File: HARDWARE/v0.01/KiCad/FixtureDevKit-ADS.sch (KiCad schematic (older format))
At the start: 54 parts, among them J16 ADS_48, J17 ADS_48, J18 ADS_4A, J19 ADS_4A, J20 ADS_48, J21 ADS_4A, J22 ADS, J23 ADS, J24 ADS_49, J25 ADS_49, J26 ADS_49, J27 ADS_4B, J28 ADS_4B, J29 ADS_4B, U1 ADS1015IDGST, U2 ADS1015IDGST, U3 ADS1015IDGST, U4 ADS1015IDGST

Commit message: more PCB layout
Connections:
- net C4-VCC-3V3: now also J16.1 (Pin_1), J17.1 (Pin_1); no longer J16.4 (Pin_4), J17.4 (Pin_4)
- net GND: now also J16.2 (Pin_2), J17.2 (Pin_2); no longer J16.3 (Pin_3), J17.3 (Pin_3)
- net I2C-SCK: now also J16.4 (Pin_4), J17.4 (Pin_4); no longer J16.1 (Pin_1), J17.1 (Pin_1)
- net I2C-SDA: now also J16.3 (Pin_3), J17.3 (Pin_3); no longer J16.2 (Pin_2), J17.2 (Pin_2)
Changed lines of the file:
@@
 L Conn_01x04 J16
 U 1 1 59F16A10
-P 1350 2800
-F 0 "J16" H 1350 3000 50  0000 C CNN
-F 1 "ADS_48" H 1350 2500 50  0000 C CNN
-F 2 "Pin_Headers:Pin_Header_Straight_1x04_Pitch2.54mm" H 1350 2800 50  0001 C CNN
-F 3 "" H 1350 2800 50  0001 C CNN
-	1    1350 2800
-	0    1    -1   0
+P 1250 2800
+F 0 "J16" H 1250 3000 50  0000 C CNN
+F 1 "ADS_48" H 1250 2500 50  0000 C CNN
+F 2 "Pin_Headers:Pin_Header_Straight_1x04_Pitch2.54mm" H 1250 2800 50  0001 C CNN
+F 3 "" H 1250 2800 50  0001 C CNN
+	1    1250 2800
+	0    -1   -1   0
 $EndComp
 Text Label 1150 3050 3    60   ~ 0
@@
 L Conn_01x04 J17
 U 1 1 59F183CB
-P 1350 4850
-F 0 "J17" H 1350 5050 50  0000 C CNN
-F 1 "ADS_48" H 1350 4550 50  0000 C CNN
-F 2 "Pin_Headers:Pin_Header_Straight_1x04_Pitch2.54mm" H 1350 4850 50  0001 C CNN
-F 3 "" H 1350 4850 50  0001 C CNN
-	1    1350 4850
-	0    1    1    0
+P 1250 4850
+F 0 "J17" H 1250 5050 50  0000 C CNN
+F 1 "ADS_48" H 1250 4550 50  0000 C CNN
+F 2 "Pin_Headers:Pin_Header_Straight_1x04_Pitch2.54mm" H 1250 4850 50  0001 C CNN
+F 3 "" H 1250 4850 50  0001 C CNN
+	1    1250 4850
+	0    -1   1    0
 $EndComp
 Text Label 1150 4600 1    60   ~ 0

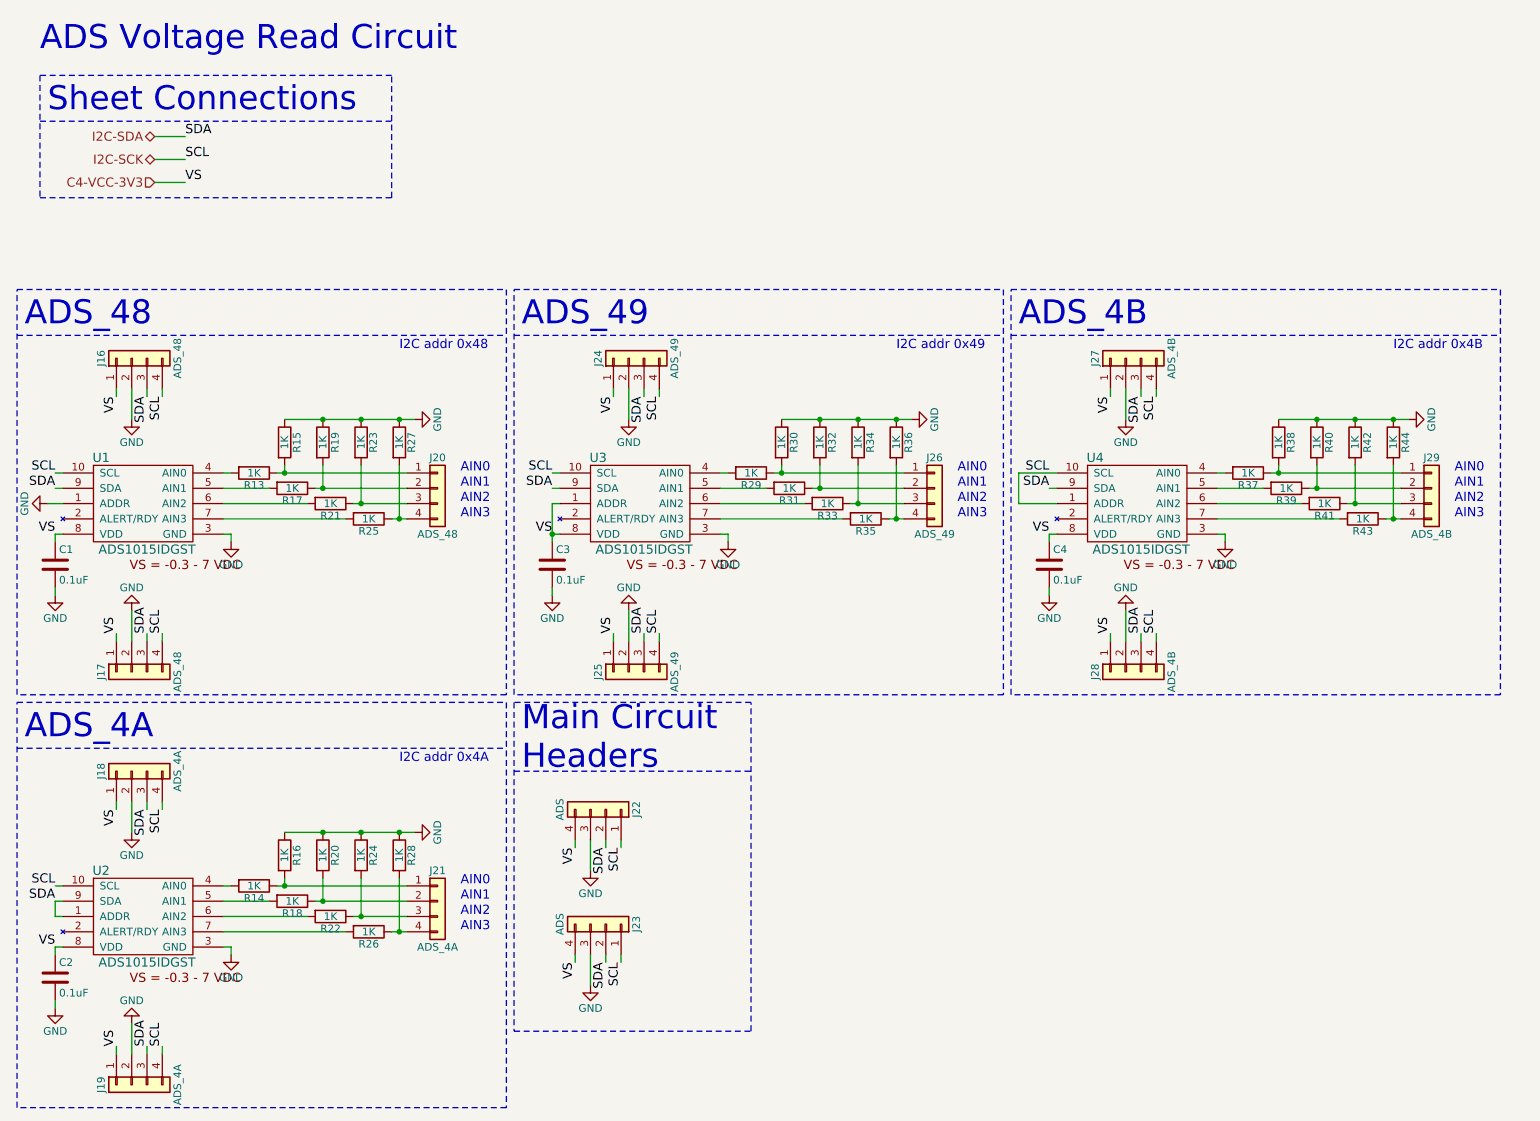
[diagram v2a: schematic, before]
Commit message: quasi-redoing entire schematic and layout
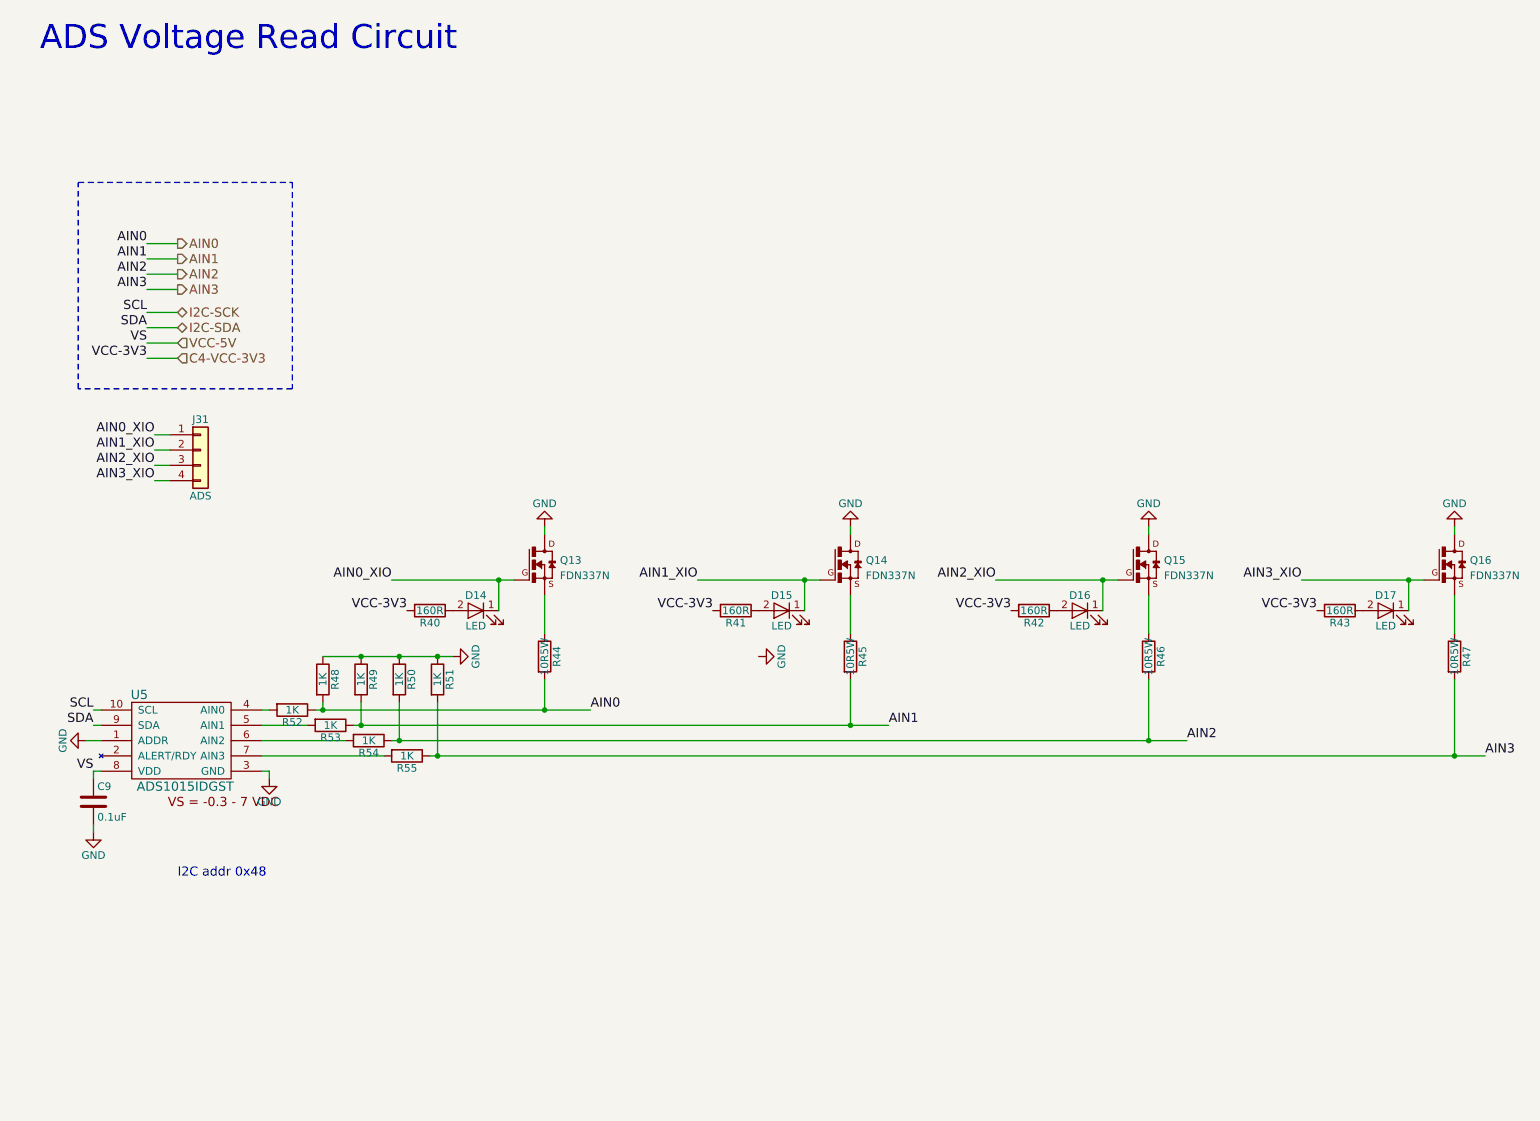
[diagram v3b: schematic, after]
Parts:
- removed C2, C3, C4: 0.1uF, Capacitors_SMD:C_0805_HandSoldering, symbol C
- removed J16, J17, J20: ADS_48, Pin_Headers:Pin_Header_Straight_1x04_Pitch2.54mm, symbol Conn_01x04
- removed J18, J19, J21: ADS_4A, Pin_Headers:Pin_Header_Straight_1x04_Pitch2.54mm, symbol Conn_01x04
- removed J22, J23: ADS, Pin_Headers:Pin_Header_Straight_1x04_Pitch2.54mm, symbol Conn_01x04
- removed J24, J25, J26: ADS_49, Pin_Headers:Pin_Header_Straight_1x04_Pitch2.54mm, symbol Conn_01x04
- removed J27, J28, J29: ADS_4B, Pin_Headers:Pin_Header_Straight_1x04_Pitch2.54mm, symbol Conn_01x04
- removed R14, R16, R18, R20, R22, R24, R26, R28, R29, R30, R31, R32, R33, R34, R35, R36, R37, R38, R39: 1K, Resistors_SMD:R_0805_HandSoldering, symbol R
- removed U2, U3, U4: ADS1015IDGST, ADS1015IDGST:SOP50P490X110-10N, symbol ADS1015IDGST
- added D14, D15, D16, D17: LED, 1206:1206, symbol LED
- added J31: ADS, Pin_Headers:Pin_Header_Straight_1x04_Pitch2.54mm, symbol Conn_01x04
- added Q13, Q14, Q15, Q16: FDN337N, FDN337N:SSOT-3, symbol FDN337N
- added R45, R46, R47: 10R5W, RES_TWM3J560E:RES_TWM3J560E, symbol R
- R40, R41, R42, R43: value 1K -> 160R
- R44: value 1K -> 10R5W; footprint Resistors_SMD:R_0805_HandSoldering -> RES_TWM3J560E:RES_TWM3J560E
- renumbered C1 to C9, R15 to R48, R19 to R49, R23 to R50, R27 to R51, R13 to R52, R17 to R53, R21 to R54, R25 to R55, U1 to U5
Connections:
- net C4-VCC-3V3: now also R40.2, R41.2, R42.2, R43.2; no longer C9.1, U5.8 (VDD)
- net GND: now also Q13.3 (D), Q14.3 (D), Q15.3 (D), Q16.3 (D); no longer R40.1, R42.1, R44.1
- net AIN0: now reaches R48.2, R52.1
- net AIN0: now also R44.2
- net AIN1: now reaches R49.2, R53.1
- net AIN1: now also R45.2
- net AIN2: now reaches R50.2, R54.1
- net AIN2: now also R46.2
- net AIN3: now reaches R51.2, R55.1
- net AIN3: now also R47.2
- net at R41.1: now also D15.2 (A); no longer R42.2
- net at R43.1: now also D17.2 (A); no longer R44.2
- new net: Q13.2 (S), R44.1
- new net: D14.2 (A), R40.1
- new net: Q14.2 (S), R45.1
- new net: Q15.2 (S), R46.1
- new net: D16.2 (A), R42.1
- new net: Q16.2 (S), R47.1
- new net AIN0_XIO: D14.1 (K), J31.1 (Pin_1), Q13.1 (G)
- new net AIN1_XIO: D15.1 (K), J31.2 (Pin_2), Q14.1 (G)
- new net AIN2_XIO: D16.1 (K), J31.3 (Pin_3), Q15.1 (G)
- new net AIN3_XIO: D17.1 (K), J31.4 (Pin_4), Q16.1 (G)
- new net VCC-5V: C9.1, U5.8 (VDD)
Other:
- note removed: "ADS_48"
- note removed: "ADS_49\n"
- note removed: "ADS_4A"
- note removed: "ADS_4B\n"
- note removed: "AIN0"
- note removed: "AIN1"
- note removed: "AIN2"
- note removed: "AIN3"
- note removed: "I2C addr 0x49"
- note removed: "I2C addr 0x4A"
- note removed: "I2C addr 0x4B"
- note removed: "Main Circuit\nHeaders"
- note removed: "Sheet Connections"
- moved on the sheet: C9, R48, R49, R50, R51, R52, R53, R54, R55, U5

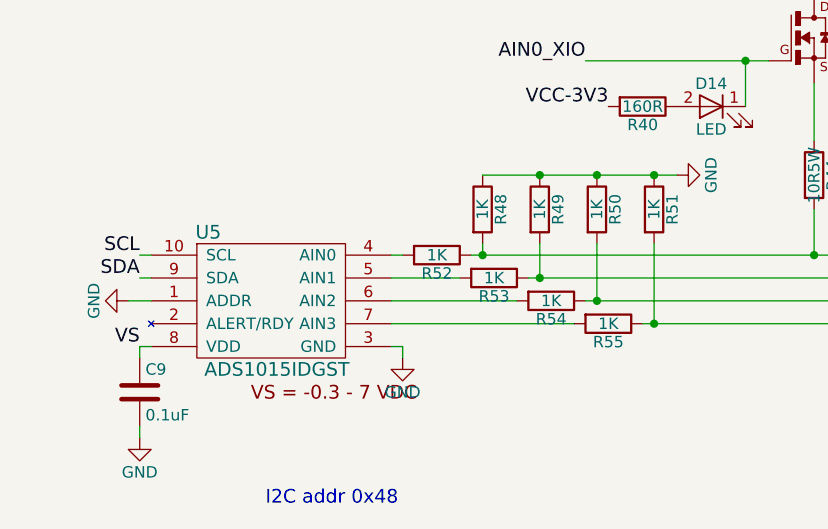
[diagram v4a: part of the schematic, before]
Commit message: updating layout footprints and board outline
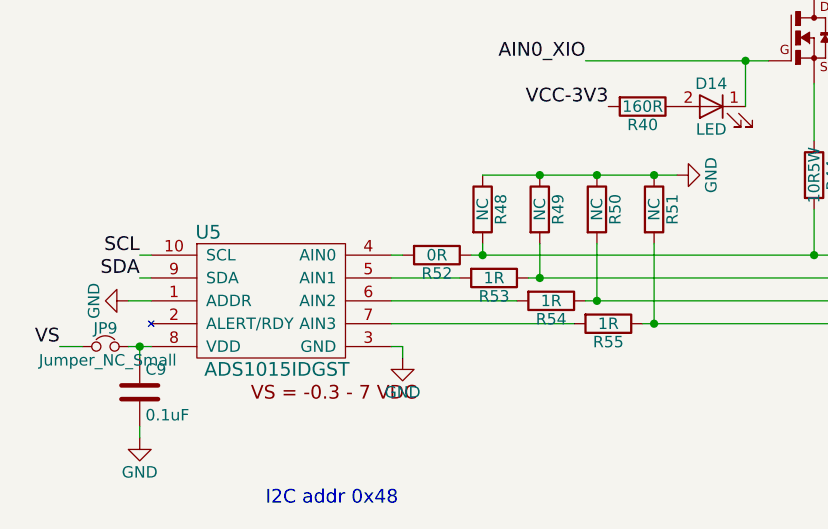
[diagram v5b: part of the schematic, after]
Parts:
- added JP9: Jumper_NC_Small, ConnectedCutJumper:connectedCutJumper, symbol Jumper_NC_Small
- R48, R49, R50, R51: value 1K -> NC
- R52: value 1K -> 0R
- R53, R54, R55: value 1K -> 1R
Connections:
- net VCC-5V: now also JP9.1; no longer C9.1, U5.8 (VDD)
- new net: C9.1, JP9.2, U5.8 (VDD)
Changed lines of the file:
@@
 Text Label 1000 5200 2    60   ~ 0
 SDA
-Text Label 1000 5500 2    60   ~ 0
+Text Label 650  5500 2    60   ~ 0
 VS
 Wire Wire Line
-	1000 5500 1050 5500
+	950  5500 1050 5500
 Wire Wire Line
 	1000 5200 1050 5200
@@
 P 2300 5100
 F 0 "R52" V 2380 5100 50  0000 C CNN
-F 1 "1K" V 2300 5100 50  0000 C CNN
+F 1 "0R" V 2300 5100 50  0000 C CNN
 F 2 "Resistors_SMD:R_0805_HandSoldering" V 2230 5100 50  0001 C CNN
 F 3 "" H 2300 5100 50  0001 C CNN
@@
 P 2500 4900
 F 0 "R48" V 2580 4900 50  0000 C CNN
-F 1 "1K" V 2500 4900 50  0000 C CNN
+F 1 "NC" V 2500 4900 50  0000 C CNN
 F 2 "Resistors_SMD:R_0805_HandSoldering" V 2430 4900 50  0001 C CNN
 F 3 "" H 2500 4900 50  0001 C CNN
@@
 P 3050 5400
 F 0 "R55" V 3130 5400 50  0000 C CNN
-F 1 "1K" V 3050 5400 50  0000 C CNN
+F 1 "1R" V 3050 5400 50  0000 C CNN
 F 2 "Resistors_SMD:R_0805_HandSoldering" V 2980 5400 50  0001 C CNN
 F 3 "" H 3050 5400 50  0001 C CNN
@@
 P 2800 5300
 F 0 "R54" V 2880 5300 50  0000 C CNN
-F 1 "1K" V 2800 5300 50  0000 C CNN
+F 1 "1R" V 2800 5300 50  0000 C CNN
 F 2 "Resistors_SMD:R_0805_HandSoldering" V 2730 5300 50  0001 C CNN
 F 3 "" H 2800 5300 50  0001 C CNN
@@
 P 2550 5200
 F 0 "R53" V 2630 5200 50  0000 C CNN
-F 1 "1K" V 2550 5200 50  0000 C CNN
+F 1 "1R" V 2550 5200 50  0000 C CNN
 F 2 "Resistors_SMD:R_0805_HandSoldering" V 2480 5200 50  0001 C CNN
 F 3 "" H 2550 5200 50  0001 C CNN
@@
 P 3250 4900
 F 0 "R51" V 3330 4900 50  0000 C CNN
-F 1 "1K" V 3250 4900 50  0000 C CNN
+F 1 "NC" V 3250 4900 50  0000 C CNN
 F 2 "Resistors_SMD:R_0805_HandSoldering" V 3180 4900 50  0001 C CNN
 F 3 "" H 3250 4900 50  0001 C CNN
@@
 P 3000 4900
 F 0 "R50" V 3080 4900 50  0000 C CNN
-F 1 "1K" V 3000 4900 50  0000 C CNN
+F 1 "NC" V 3000 4900 50  0000 C CNN
 F 2 "Resistors_SMD:R_0805_HandSoldering" V 2930 4900 50  0001 C CNN
 F 3 "" H 3000 4900 50  0001 C CNN
@@
 P 2750 4900
 F 0 "R49" V 2830 4900 50  0000 C CNN
-F 1 "1K" V 2750 4900 50  0000 C CNN
+F 1 "NC" V 2750 4900 50  0000 C CNN
 F 2 "Resistors_SMD:R_0805_HandSoldering" V 2680 4900 50  0001 C CNN
 F 3 "" H 2750 4900 50  0001 C CNN
@@
 Wire Wire Line
 	1350 2800 1550 2800
+$Comp
+L Jumper_NC_Small JP9
+U 1 1 59F9B52B
+P 850 5500
+F 0 "JP9" H 850 5580 50  0000 C CNN
+F 1 "Jumper_NC_Small" H 860 5440 50  0000 C CNN
+F 2 "ConnectedCutJumper:connectedCutJumper" H 850 5500 50  0001 C CNN
+F 3 "" H 850 5500 50  0001 C CNN
+	1    850  5500
+	1    0    0    -1
+$EndComp
+Connection ~ 1000 5500
+Wire Wire Line
+	750  5500 650  5500
 $EndSCHEMATC
